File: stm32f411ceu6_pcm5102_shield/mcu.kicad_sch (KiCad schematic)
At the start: 1 part

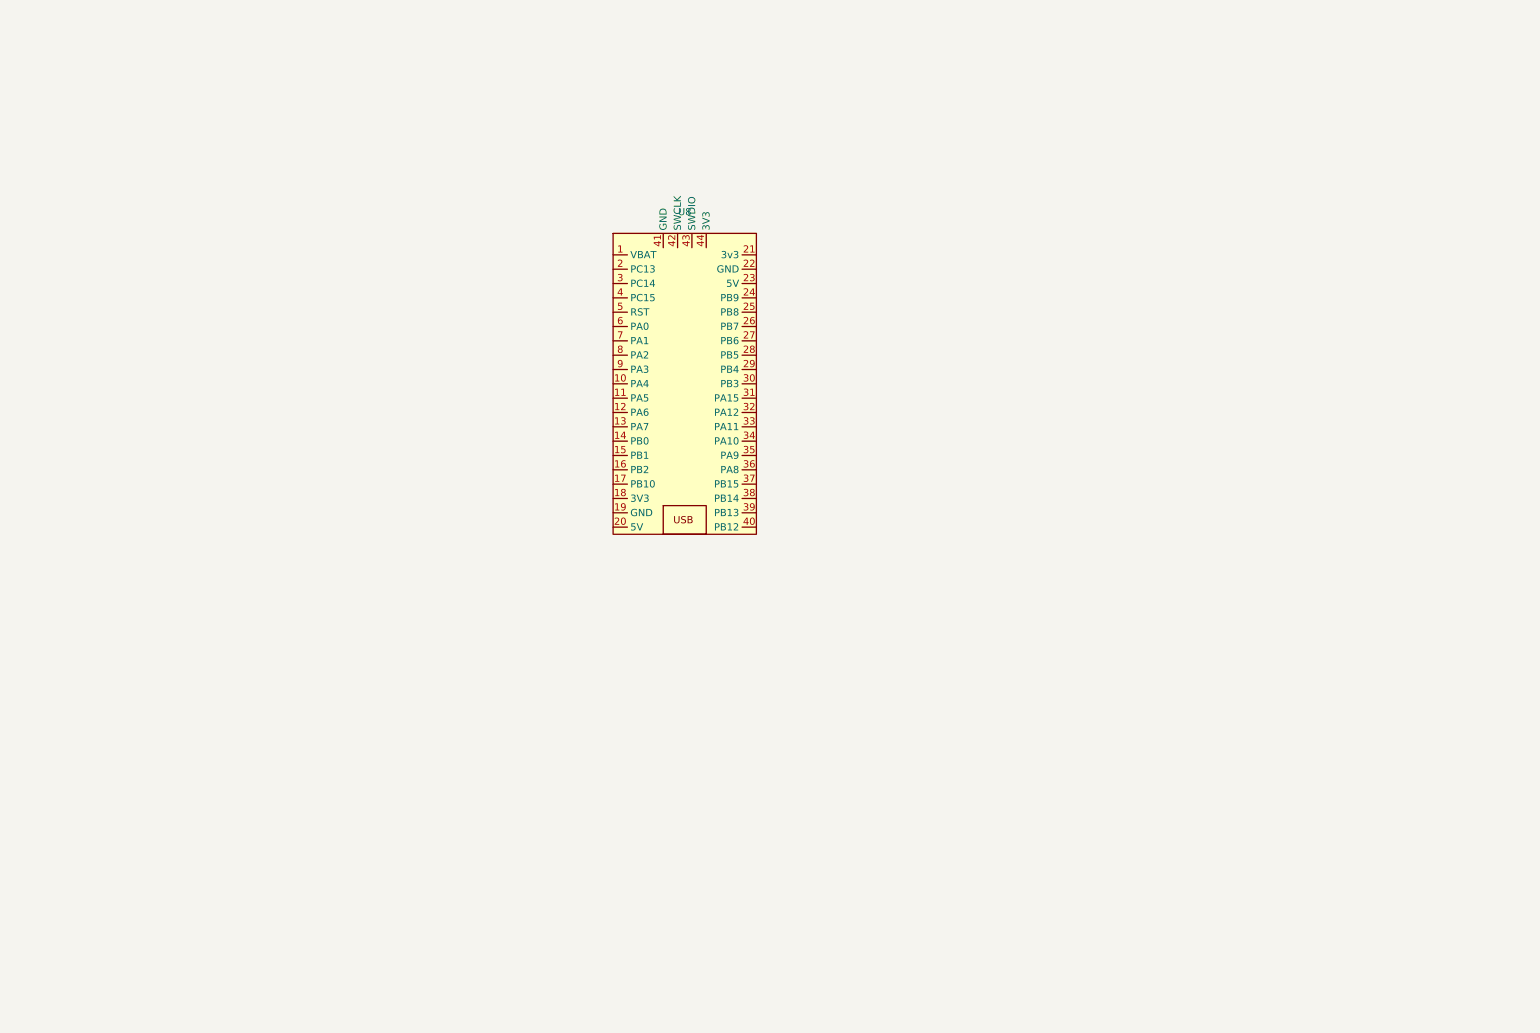
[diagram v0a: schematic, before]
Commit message: Placed all components on the board
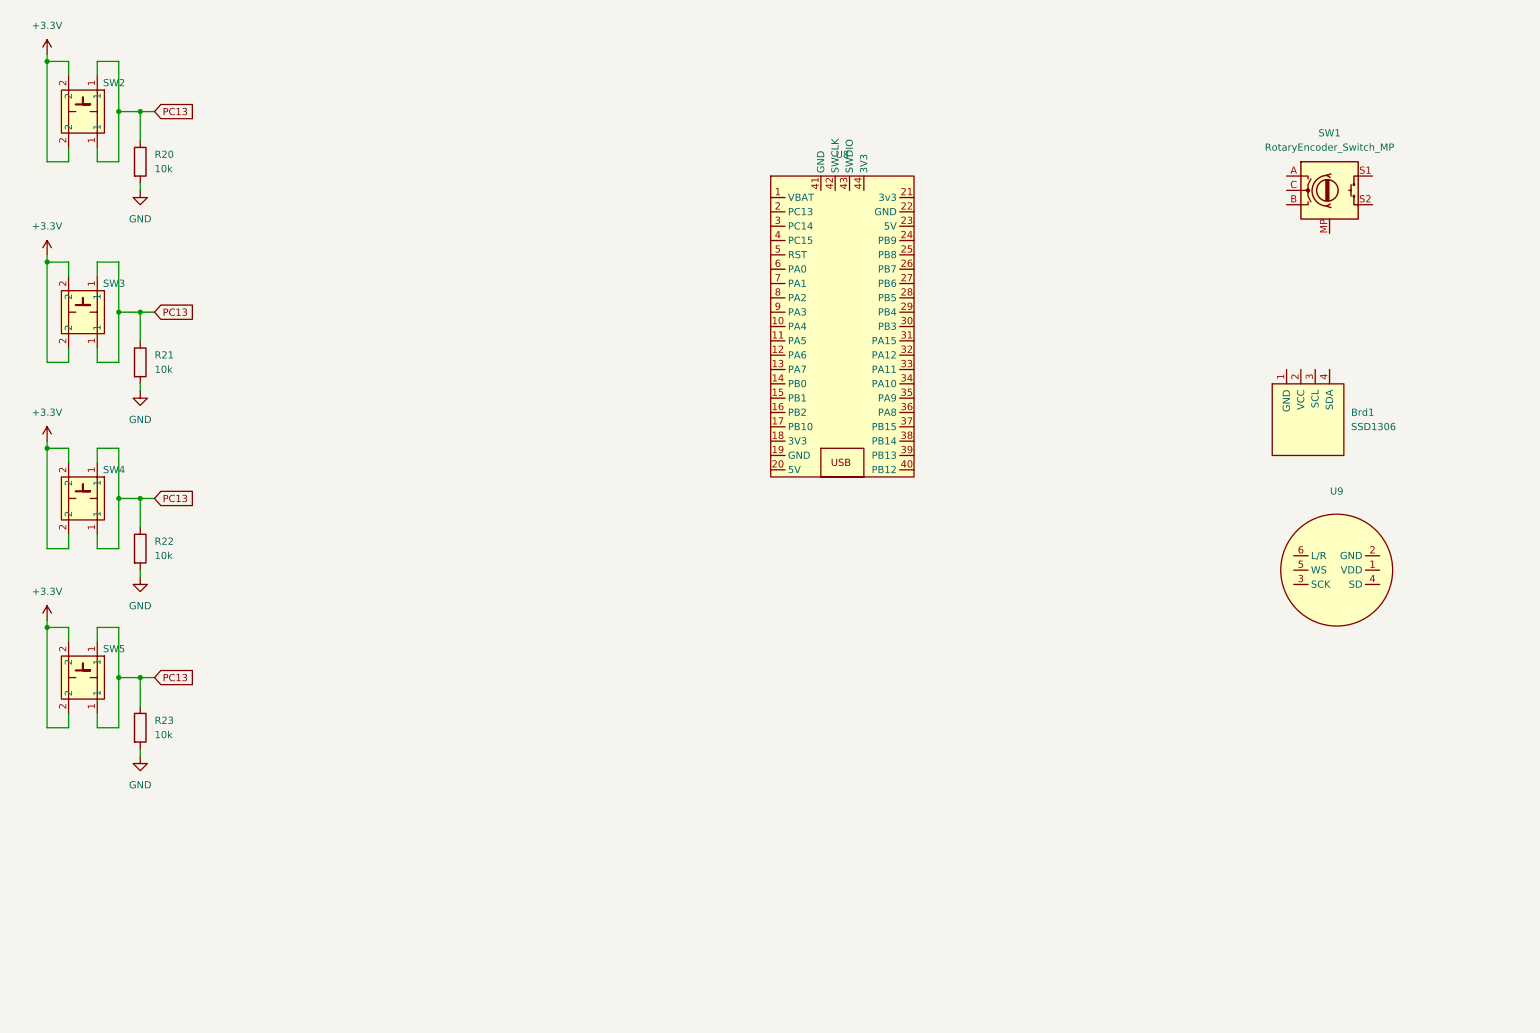
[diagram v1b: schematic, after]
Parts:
- added Brd1: SSD1306, stm32f401_pcm5102_shiled_lib:128x64OLED, symbol stm32f401_pcm5102_shiled_lib:SSD1306
- added R20, R21, R22, R23: 10k, Resistor_SMD:R_0402_1005Metric, symbol Device:R
- added SW1: RotaryEncoder_Switch_MP, Rotary_Encoder:RotaryEncoder_Alps_EC12E-Switch_Vertical_H20mm, symbol Device:RotaryEncoder_Switch_MP
- added SW2, SW3, SW4, SW5: ~, Button_Switch_THT:SW_PUSH_6mm, symbol BlackPillLibrary:SW_PUSH_6mm_H5mm
- added U9: ~, stm32f401_pcm5102_shiled_lib:inmp441, symbol stm32f401_pcm5102_shiled_lib:inmp441
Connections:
- new net +3.3V: SW2.2, SW3.2, SW4.2, SW5.2
- new net GND: R20.2, R21.2, R22.2, R23.2
- new net PC13: R20.1, R21.1, R22.1, R23.1, SW2.1, SW3.1, SW4.1, SW5.1
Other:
- moved on the sheet: U8

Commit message: Add rotary encoder
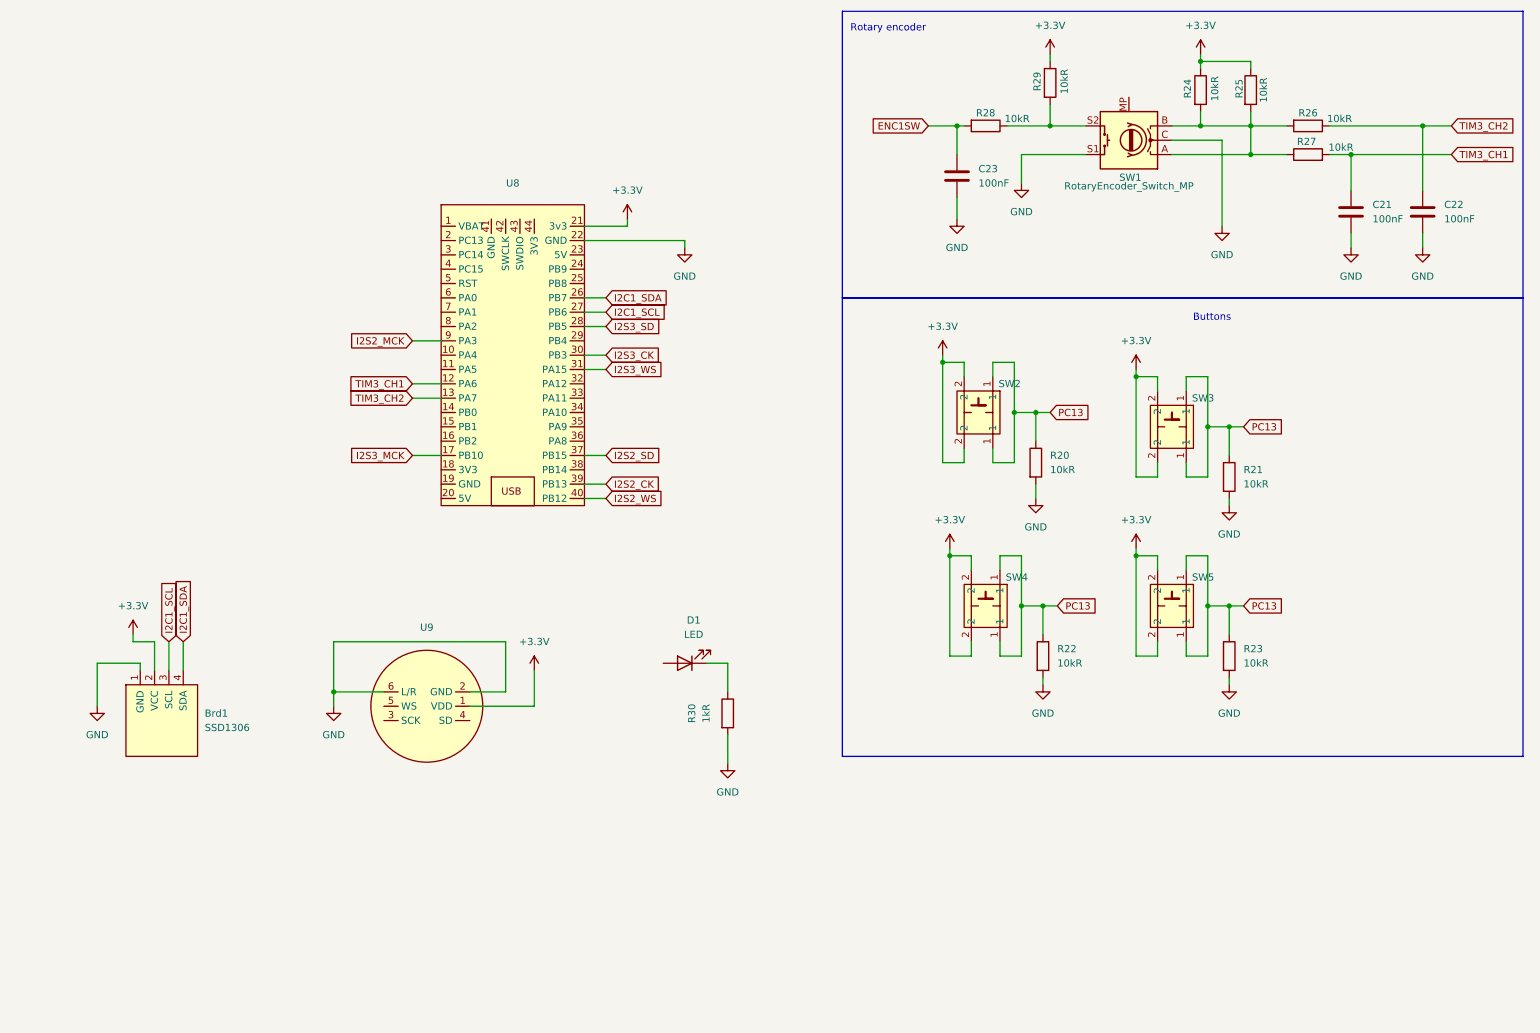
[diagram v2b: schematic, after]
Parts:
- added C21, C22, C23: 100nF, Capacitor_SMD:C_0805_2012Metric, symbol Device:C
- added D1: LED, LED_THT:LED_D3.0mm, symbol Device:LED
- added R24, R25, R26, R27, R28, R29: 10kR, Resistor_SMD:R_0805_2012Metric, symbol Device:R
- added R30: 1kR, Resistor_SMD:R_0805_2012Metric, symbol Device:R
- R20, R21, R22, R23: value 10k -> 10kR
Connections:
- net +3.3V: now also Brd1.2 (VCC), U8.21 (3v3), U9.1 (VDD), R24.1, R25.1, R29.1
- net GND: now also Brd1.1 (GND), SW1.C, SW1.S1, U8.22 (GND), U9.2 (GND), U9.6 (L/R), C21.2, C22.2, C23.2, R30.2
- net TIM3_CH1: now reaches U8.12 (PA6)
- net TIM3_CH1: now also C21.1, R27.2
- net TIM3_CH2: now reaches U8.13 (PA7)
- net TIM3_CH2: now also C22.1, R26.1
- net I2S3_MCK: now reaches U8.17 (PB10)
- net I2C1_SDA: now reaches U8.26 (PB7)
- net I2C1_SDA: now also Brd1.4 (SDA)
- net I2C1_SCL: now reaches U8.27 (PB6)
- net I2C1_SCL: now also Brd1.3 (SCL)
- net I2S3_SD: now reaches U8.28 (PB5)
- net I2S3_CK: now reaches U8.30 (PB3)
- net I2S3_WS: now reaches U8.31 (PA15)
- net I2S2_SD: now reaches U8.37 (PB15)
- net I2S2_CK: now reaches U8.39 (PB13)
- net I2S2_WS: now reaches U8.40 (PB12)
- net I2S2_MCK: now reaches U8.9 (PA3)
- net at SW1.A: now also SW1.B, R24.2, R25.2, R26.2, R27.1
- net at SW1.S2: now also R28.1, R29.2
- new net: D1.1 (K), R30.1
- new net ENC1SW: C23.1, R28.2
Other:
- note added: "Buttons"
- note added: "Rotary encoder"
- moved on the sheet: Brd1, R20, R21, R22, R23, SW1, SW2, SW3, SW4, SW5, U8, U9

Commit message: Alignment of ST project to the scheme
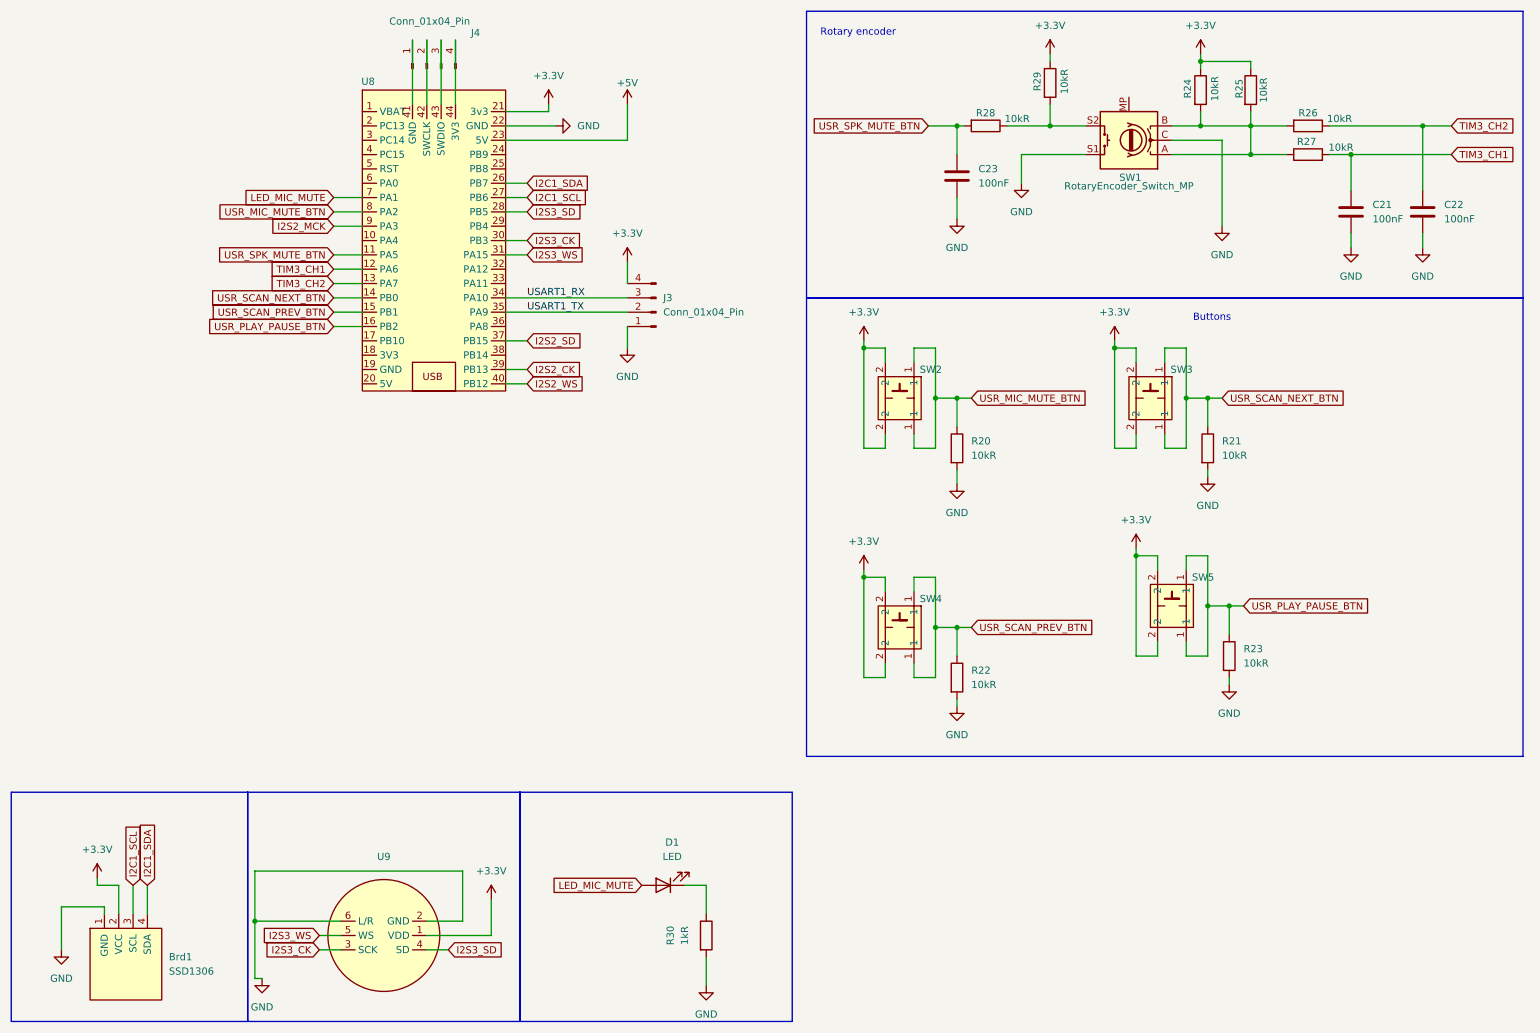
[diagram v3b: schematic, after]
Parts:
- added J3, J4: Conn_01x04_Pin, Connector_PinHeader_2.54mm:PinHeader_1x04_P2.54mm_Vertical, symbol Connector:Conn_01x04_Pin
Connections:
- net ENC1SW is gone; now on net USR_SPK_MUTE_BTN: C23.1, R28.2
- net +3.3V: now also J3.4 (Pin_4)
- net GND: now also J3.1 (Pin_1)
- net I2S3_CK: now also U9.3 (SCK)
- net I2S3_SD: now also U9.4 (SD)
- net I2S3_WS: now also U9.5 (WS)
- net USR_SPK_MUTE_BTN: now reaches U8.11 (PA5)
- net USR_SCAN_NEXT_BTN: now reaches U8.14 (PB0)
- net USR_SCAN_NEXT_BTN: now also R21.1, SW3.1
- net USR_SCAN_PREV_BTN: now reaches U8.15 (PB1)
- net USR_SCAN_PREV_BTN: now also R22.1, SW4.1
- net USR_PLAY_PAUSE_BTN: now reaches U8.16 (PB2)
- net USR_PLAY_PAUSE_BTN: now also R23.1, SW5.1
- net +5V: now reaches U8.23 (5V)
- net USART1_RX: now reaches U8.34 (PA10)
- net USART1_RX: now also J3.3 (Pin_3)
- net USART1_TX: now reaches U8.35 (PA9)
- net USART1_TX: now also J3.2 (Pin_2)
- net at U8.41 (GND): now also J4.1 (Pin_1)
- net at U8.42 (SWCLK): now also J4.2 (Pin_2)
- net at U8.43 (SWDIO): now also J4.3 (Pin_3)
- net at U8.44 (3V3): now also J4.4 (Pin_4)
- net LED_MIC_MUTE: now reaches U8.7 (PA1)
- net LED_MIC_MUTE: now also D1.2 (A)
- net USR_MIC_MUTE_BTN: now reaches U8.8 (PA2)
- net USR_MIC_MUTE_BTN: now also R20.1, SW2.1
- net I2S3_MCK: no longer names the net of U8.17 (PB10)
- removed net PC13: R20.1, R21.1, R22.1, R23.1, SW2.1, SW3.1, SW4.1, SW5.1
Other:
- moved on the sheet: Brd1, D1, R20, R21, R22, R30, SW2, SW3, SW4, U8, U9
